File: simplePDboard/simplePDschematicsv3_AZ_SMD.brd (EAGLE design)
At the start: 28 x 28 mm, 15 parts, among them IC1 TL071P

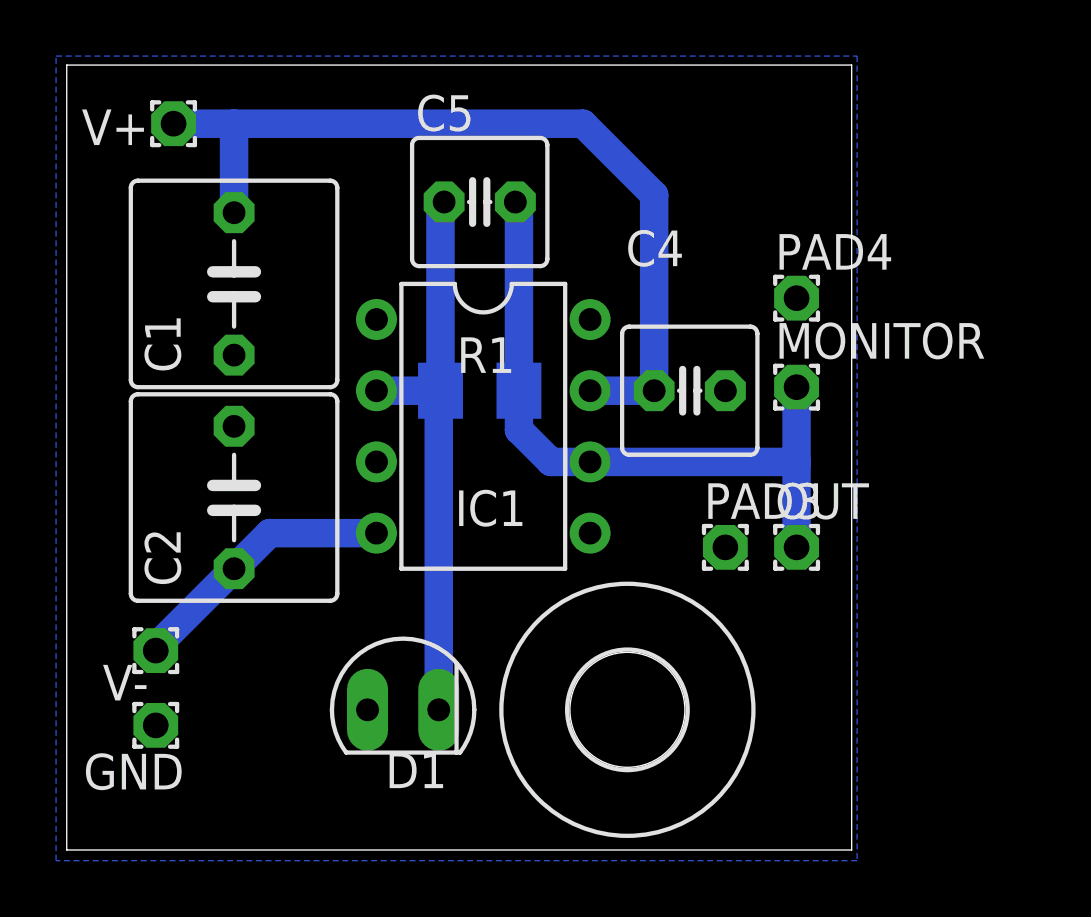
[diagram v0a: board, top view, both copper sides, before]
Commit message: Updated the simplePD board. — It is not in photovoltaic mode. — The capacitors are better located. — We added a serial resistor for 50Ohm termination. — The power connectors are closer by.
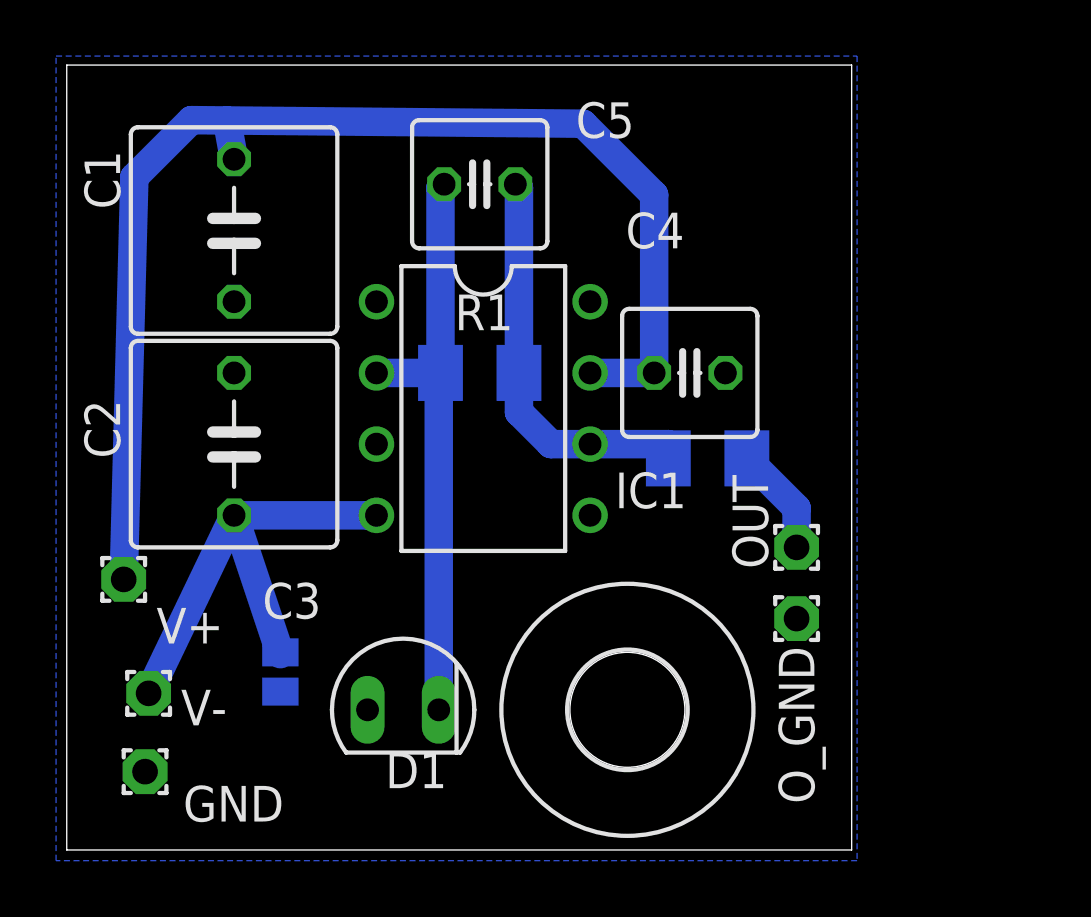
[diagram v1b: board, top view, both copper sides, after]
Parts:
- removed MONITOR, PAD3, PAD4: (no value), wirepad:1,6/0,9
- added C3: (no value), resistor:C0504
- added O_GND: (no value), wirepad:1,6/0,9
- added R2: 50, resistor:M1206
- moved V+ 16.4 mm to (2.03, 9.65), turned to 90 degrees
- moved C2 1.90 mm to (5.97, 14.5)
- moved C1 1.90 mm to (5.97, 22.1)
- moved GND 1.69 mm to (2.79, 2.79)
- moved V- 1.55 mm to (2.92, 5.59)
- moved C4 0.64 mm to (22.2, 17.0)
- moved R1 0.64 mm to (14.7, 17.0)
- moved IC1 0.63 mm to (14.9, 15.7)
- moved C5 0.63 mm to (14.7, 23.7)
- turned OUT to 90 degrees
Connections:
- new net N$1: OUT.1, R2.2
- net GND: now also O_GND.1; no longer PAD3.1, PAD4.1
- net N$2: now also R2.1; no longer MONITOR.1, OUT.1
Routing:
- net V+: track 30.6 -> 44.8 mm
- net N$2: track 24.3 -> 14.5 mm
- net V-: track 10.0 -> 17.7 mm
- net N$1: track 0.00 -> 3.91 mm
- net N$3: track 20.5 -> 21.1 mm
